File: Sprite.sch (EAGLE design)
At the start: 32 parts, among them P1 SPRITE_PIN, P2 SPRITE_PIN, U1 CC430F5137, U2 HMC5883LSMD, U3 ITG-3200, X1 TCXO_7Z

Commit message: Rolled my own motor driver
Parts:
- removed C10, C8: 100nF, SparkFun:CAP0603-CAP
- removed C11: 220nF, SparkFun:CAP0603-CAP
- removed C12: 4.7uF, SparkFun:CAP0603-CAP
- removed C7: 2.2nF, SparkFun:CAP0603-CAP
- removed C9: 10nF, SparkFun:CAP0603-CAP
- removed R3, R4: 4.7K, SparkFun:RESISTOR0603-RES
- removed U3: ITG-3200, SparkFun:ITG-3200
- added S3, S4: TRISOLX-WING, TriSolX_QzQube:TRISOLX-WING
- S1, S2: value TASC -> TRISOLX-WING; device TASC:TASC -> TriSolX_QzQube:TRISOLX-WING
- U2: value HMC5883LSMD -> LSM9DS1; device SparkFun:HMC5883LSMD -> LSM9DS1:LSM9DS1
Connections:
- removed net N$10: R5.2, U1.5
- removed net N$5: C11.1, U2.SETP
- removed net N$6: C11.2, U2.SETC
- removed net N$7: C12.1, U2.C1
- removed net N$8: C7.1, U3.CPOUT
- removed net N$9: C8.1, U3.REGOUT
- removed net RXD: JP3.2, U1.12
- removed net TXD: JP3.1, U1.11
- new net N$2: R5.2, U1.14
- new net UART_RX: JP3.2, U1.6
- new net UART_TX: JP3.1, U1.5
- net GND: now also S1.A, S2.A, S3.A, S4.A; no longer C10.2, C12.2, C7.2, C8.2, C9.2, S1.MINUS1, S1.MINUS2, S2.MINUS1, S2.MINUS2, U2.GND@1, U2.GND@2, U3.AD0, U3.CLKIN, U3.GND, U3.RESV-G
- net SCL: now also U1.9; no longer R4.1, U1.3, U2.SCL, U3.SCL
- net SDA: now also U1.10; no longer R3.1, U1.2, U2.SDA, U3.SDA
- net VCC: no longer C10.1, C9.1, R3.2, R4.2, U2.S1, U2.VDD, U2.VDDIO, U3.VDD, U3.VLOGIC
- net VSOLAR: now also S1.C, S2.C, S3.C, S4.C; no longer S1.PLUS, S2.PLUS

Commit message: Revert "Rolled my own motor driver"
This reverts commit 8d15a71afd97314b3e3036af91b9c243df8797f7.
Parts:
- removed S3, S4: TRISOLX-WING, TriSolX_QzQube:TRISOLX-WING
- added C10, C8: 100nF, SparkFun:CAP0603-CAP
- added C11: 220nF, SparkFun:CAP0603-CAP
- added C12: 4.7uF, SparkFun:CAP0603-CAP
- added C7: 2.2nF, SparkFun:CAP0603-CAP
- added C9: 10nF, SparkFun:CAP0603-CAP
- added R3, R4: 4.7K, SparkFun:RESISTOR0603-RES
- added U3: ITG-3200, SparkFun:ITG-3200
- S1, S2: value TRISOLX-WING -> TASC; device TriSolX_QzQube:TRISOLX-WING -> TASC:TASC
- U2: value LSM9DS1 -> HMC5883LSMD; device LSM9DS1:LSM9DS1 -> SparkFun:HMC5883LSMD
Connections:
- removed net N$2: R5.2, U1.14
- removed net UART_RX: JP3.2, U1.6
- removed net UART_TX: JP3.1, U1.5
- new net N$10: R5.2, U1.5
- new net N$5: C11.1, U2.SETP
- new net N$6: C11.2, U2.SETC
- new net N$7: C12.1, U2.C1
- new net N$8: C7.1, U3.CPOUT
- new net N$9: C8.1, U3.REGOUT
- new net RXD: JP3.2, U1.12
- new net TXD: JP3.1, U1.11
- net GND: now also C10.2, C12.2, C7.2, C8.2, C9.2, S1.MINUS1, S1.MINUS2, S2.MINUS1, S2.MINUS2, U2.GND@1, U2.GND@2, U3.AD0, U3.CLKIN, U3.GND, U3.RESV-G; no longer S1.A, S2.A, S3.A, S4.A
- net SCL: now also R4.1, U1.3, U2.SCL, U3.SCL; no longer U1.9
- net SDA: now also R3.1, U1.2, U2.SDA, U3.SDA; no longer U1.10
- net VCC: now also C10.1, C9.1, R3.2, R4.2, U2.S1, U2.VDD, U2.VDDIO, U3.VDD, U3.VLOGIC
- net VSOLAR: now also S1.PLUS, S2.PLUS; no longer S1.C, S2.C, S3.C, S4.C

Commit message: Sprite layout with TrisolX
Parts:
- removed C11: 220nF, SparkFun:CAP0603-CAP
- removed C12: 4.7uF, SparkFun:CAP0603-CAP
- removed R3, R4: 4.7K, SparkFun:RESISTOR0603-RES
- removed R6: 0, rcl:R-US_R0805
- removed U3: ITG-3200, SparkFun:ITG-3200
- added S3, S4: TRISOLX-WING, TriSolX_QzQube:TRISOLX-WING
- C10: value 100nF -> 10uF
- C7: value 2.2nF -> 10nF
- C8: value 100nF -> 0.1uF
- C9: value 10nF -> 0.1uF
- S1, S2: value TASC -> TRISOLX-WING; device TASC:TASC -> TriSolX_QzQube:TRISOLX-WING
- U2: value HMC5883LSMD -> LSM9DS1; device SparkFun:HMC5883LSMD -> LSM9DS1:LSM9DS1
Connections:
- removed net N$10: R5.2, U1.5
- removed net N$7: C12.1, U2.C1
- removed net N$8: C7.1, U3.CPOUT
- removed net N$9: C8.1, U3.REGOUT
- removed net RXD: JP3.2, U1.12
- removed net TXD: JP3.1, U1.11
- removed net VSOLAR: R6.1, S1.PLUS, S2.PLUS
- new net N$2: R5.2, U1.14
- new net UART_RX: JP3.2, U1.6
- new net UART_TX: JP3.1, U1.5
- net GND: now also P2.PIN, S1.A, S2.A, S3.A, S4.A, U2.GND, U2.RES; no longer C12.2, S1.MINUS1, S1.MINUS2, S2.MINUS1, S2.MINUS2, U2.GND@1, U2.GND@2, U3.AD0, U3.CLKIN, U3.GND, U3.RESV-G
- net N$5: now also C7.1, U2.CAP; no longer C11.1, U2.SETP
- net N$6: now also C8.1, U2.C1; no longer C11.2, U2.SETC
- net SCL: now also U1.9, U2.SCL/SPC; no longer R4.1, U1.3, U2.SCL, U3.SCL
- net SDA: now also U1.10, U2.SDA/SDI/SDO; no longer R3.1, U1.2, U2.SDA, U3.SDA
- net VCC: now also P1.PIN, S1.C, S2.C, S3.C, S4.C, U2.CS_A/G, U2.CS_M, U2.SDO_A/G, U2.SDO_M; no longer R3.2, R4.2, R6.2, U2.S1, U3.VDD, U3.VLOGIC

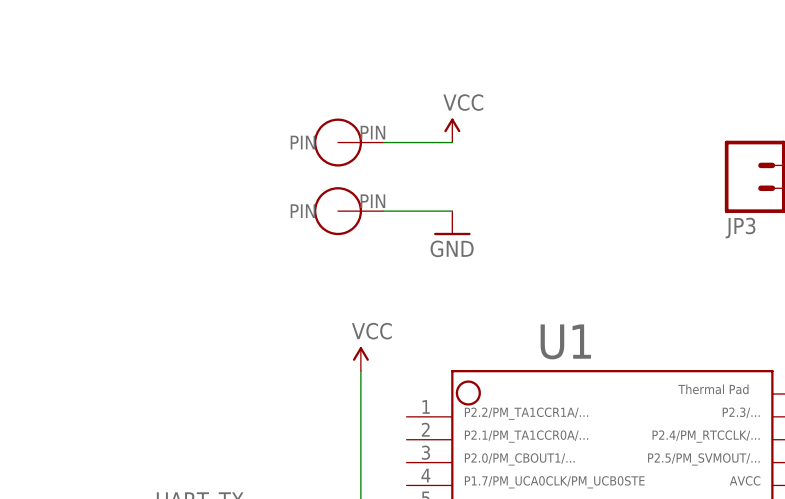
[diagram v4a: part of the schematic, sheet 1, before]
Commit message: Swapped pins
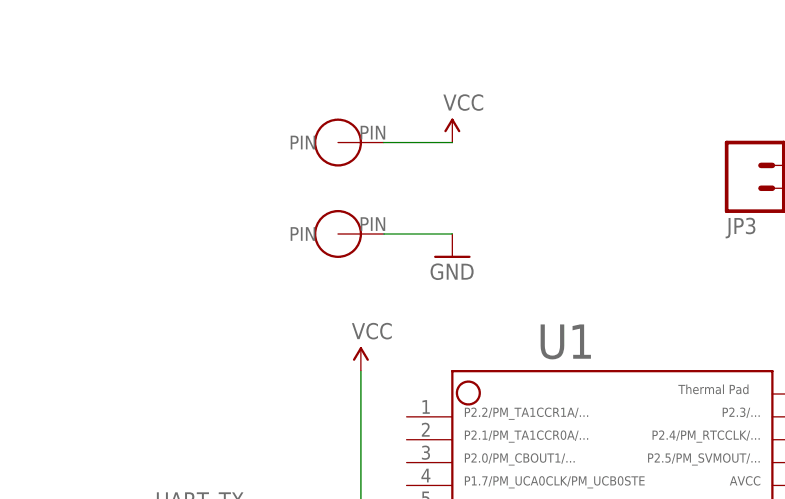
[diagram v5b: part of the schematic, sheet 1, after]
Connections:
- net GND: now also P1.PIN; no longer P2.PIN
- net VCC: now also P2.PIN; no longer P1.PIN
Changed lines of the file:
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@@
 <instance part="P+2" gate="1" x="193.04" y="106.68"/>
 <instance part="JP2" gate="G$1" x="248.92" y="93.98" rot="R180"/>
-<instance part="GND16" gate="1" x="134.62" y="134.62"/>
+<instance part="GND16" gate="1" x="134.62" y="132.08"/>
 <instance part="P+4" gate="1" x="134.62" y="144.78"/>
 <instance part="ANT-N" gate="G$1" x="231.14" y="76.2"/>
@@
 <instance part="X1" gate="G$1" x="241.3" y="50.8" rot="MR0"/>
 <instance part="P+11" gate="1" x="251.46" y="48.26"/>
-<instance part="P1" gate="G$1" x="121.92" y="144.78"/>
-<instance part="P2" gate="G$1" x="121.92" y="137.16"/>
+<instance part="P1" gate="G$1" x="121.92" y="134.62"/>
+<instance part="P2" gate="G$1" x="121.92" y="144.78"/>
 <instance part="S1" gate="G$1" x="340.36" y="93.98" rot="R90"/>
 <instance part="S2" gate="G$1" x="355.6" y="93.98" rot="R90"/>
@@
 </segment>
 <segment>
-<pinref part="P+4" gate="1" pin="VCC"/>
-<wire x1="134.62" y1="144.78" x2="127" y2="144.78" width="0.1524" layer="91"/>
-<pinref part="P1" gate="G$1" pin="PIN"/>
-</segment>
-<segment>
 <pinref part="U1" gate="G$1" pin="34"/>
 <wire x1="175.26" y1="78.74" x2="182.88" y2="78.74" width="0.1524" layer="91"/>
@@
 <wire x1="261.62" y1="144.78" x2="261.62" y2="137.16" width="0.1524" layer="91"/>
 <pinref part="C10" gate="G$1" pin="1"/>
+</segment>
+<segment>
+<pinref part="P2" gate="G$1" pin="PIN"/>
+<pinref part="P+4" gate="1" pin="VCC"/>
+<wire x1="127" y1="144.78" x2="134.62" y2="144.78" width="0.1524" layer="91"/>
 </segment>
 </net>
@@
 </segment>
 <segment>
-<pinref part="GND16" gate="1" pin="GND"/>
-<wire x1="134.62" y1="137.16" x2="127" y2="137.16" width="0.1524" layer="91"/>
-<pinref part="P2" gate="G$1" pin="PIN"/>
-</segment>
-<segment>
 <pinref part="GND7" gate="1" pin="GND"/>
 <pinref part="C2" gate="G$1" pin="2"/>
@@
 <pinref part="GND13" gate="1" pin="GND"/>
 </segment>
+<segment>
+<pinref part="P1" gate="G$1" pin="PIN"/>
+<pinref part="GND16" gate="1" pin="GND"/>
+<wire x1="127" y1="134.62" x2="134.62" y2="134.62" width="0.1524" layer="91"/>
+</segment>
 </net>
